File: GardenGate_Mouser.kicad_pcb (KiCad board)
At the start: 2 copper layers, 108 x 50.3 mm, 42 parts, among them IC1 PIC12F1822-I_SN, J2 1841513, J3 61300611121, J4 2464, K1 G3VM-61VY2, K2 G3VM-61VY2, K3 G3VM-61VY2, K4 G3VM-61VY2, U1 DRV5032AJDBZR, U2 DRV5032AJDBZR

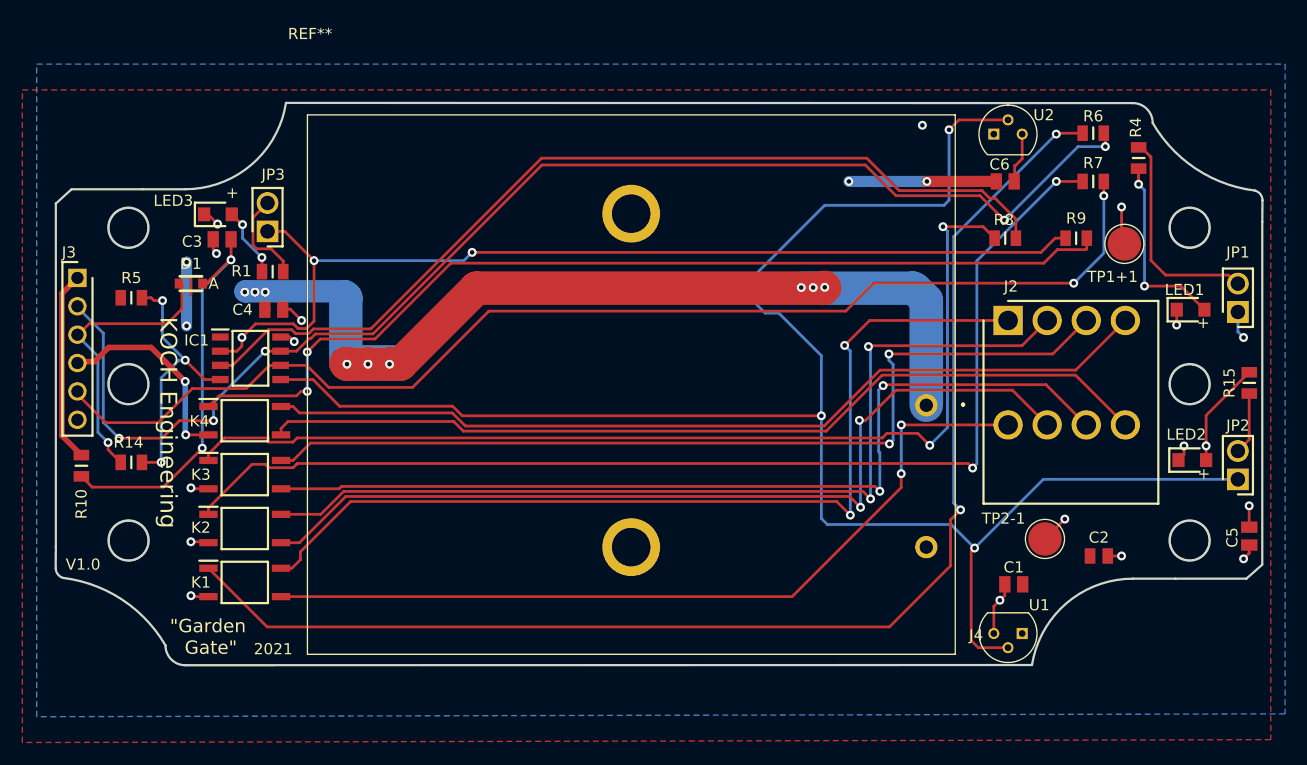
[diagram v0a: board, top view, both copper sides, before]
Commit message: A new commit with all the files from the KiCad folder
This means that some files from the Zip file has now been over written
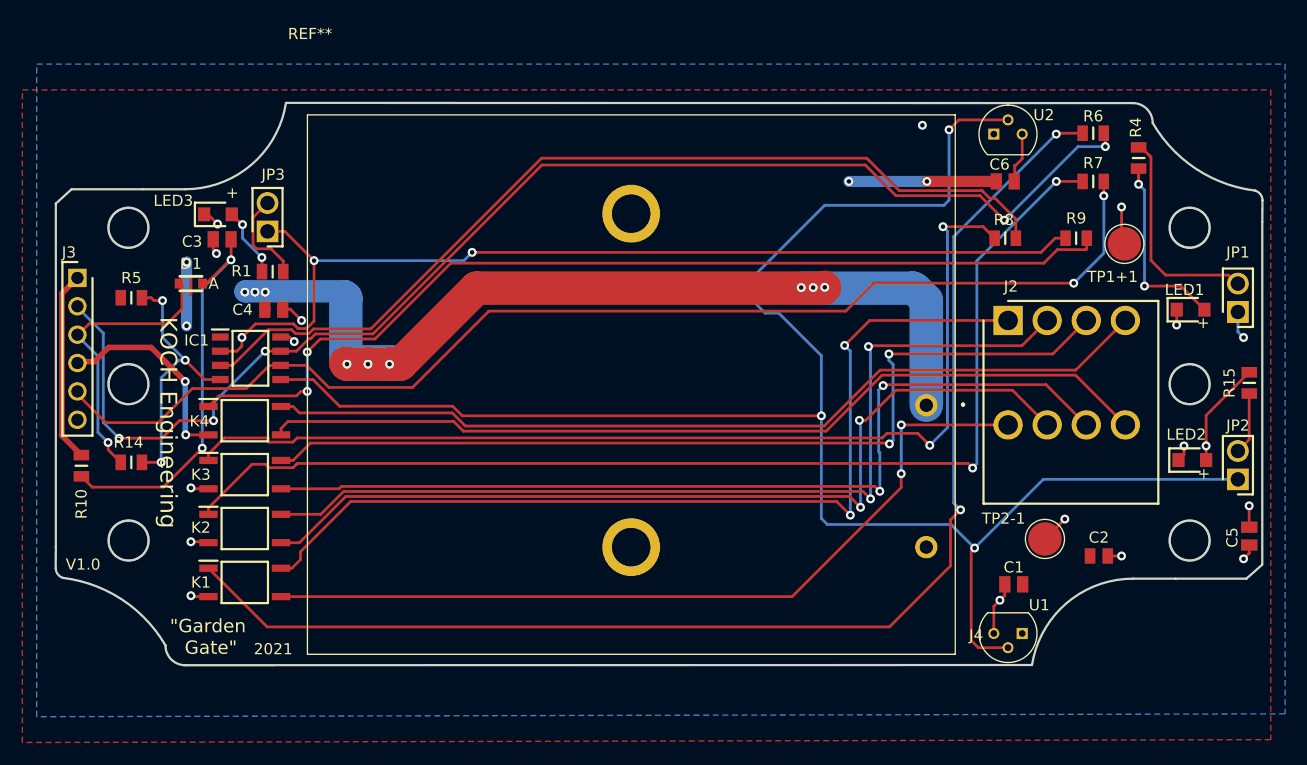
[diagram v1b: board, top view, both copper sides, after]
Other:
- net class Default removed
